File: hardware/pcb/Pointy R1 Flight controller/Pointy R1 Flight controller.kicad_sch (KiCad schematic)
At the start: 9 parts, among them IC1 TEENSY_4.1, Q1 2N7002, Q2 2N7002, Q3 2N7002, U1 L7805CV, U2 GY-521, U3 MPL3115A2

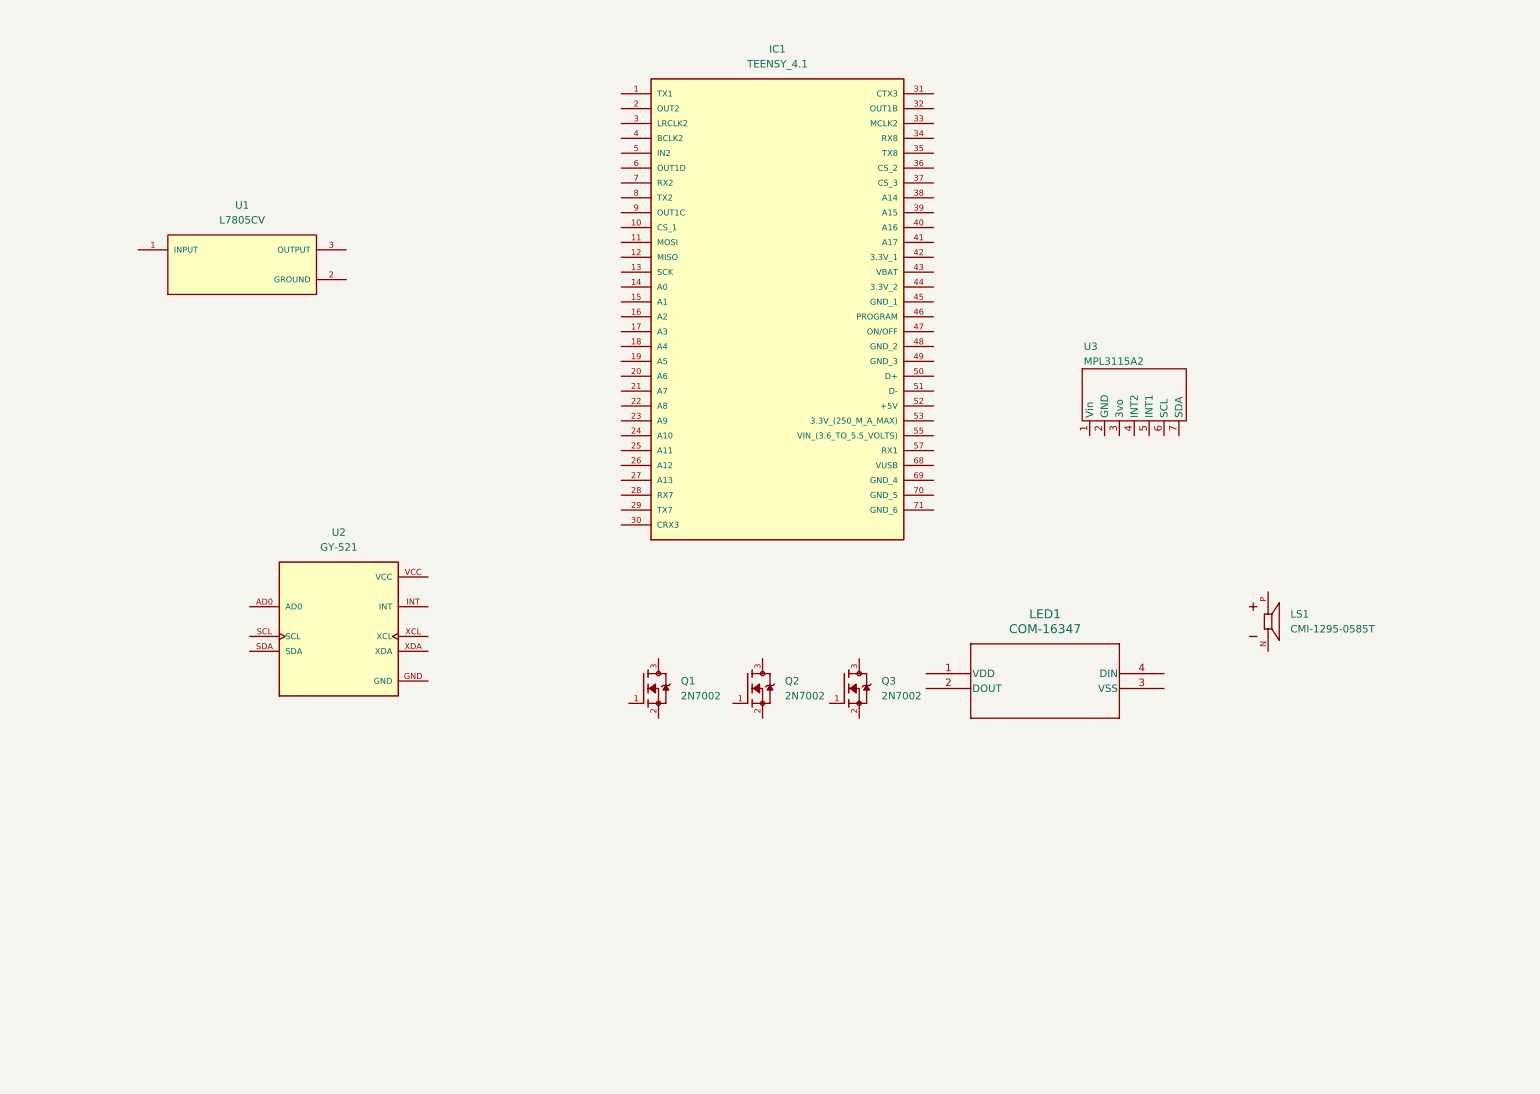
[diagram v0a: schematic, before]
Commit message: added majority of power connections + buses, wired MPL3115A2 altimeter and gy-521 imu
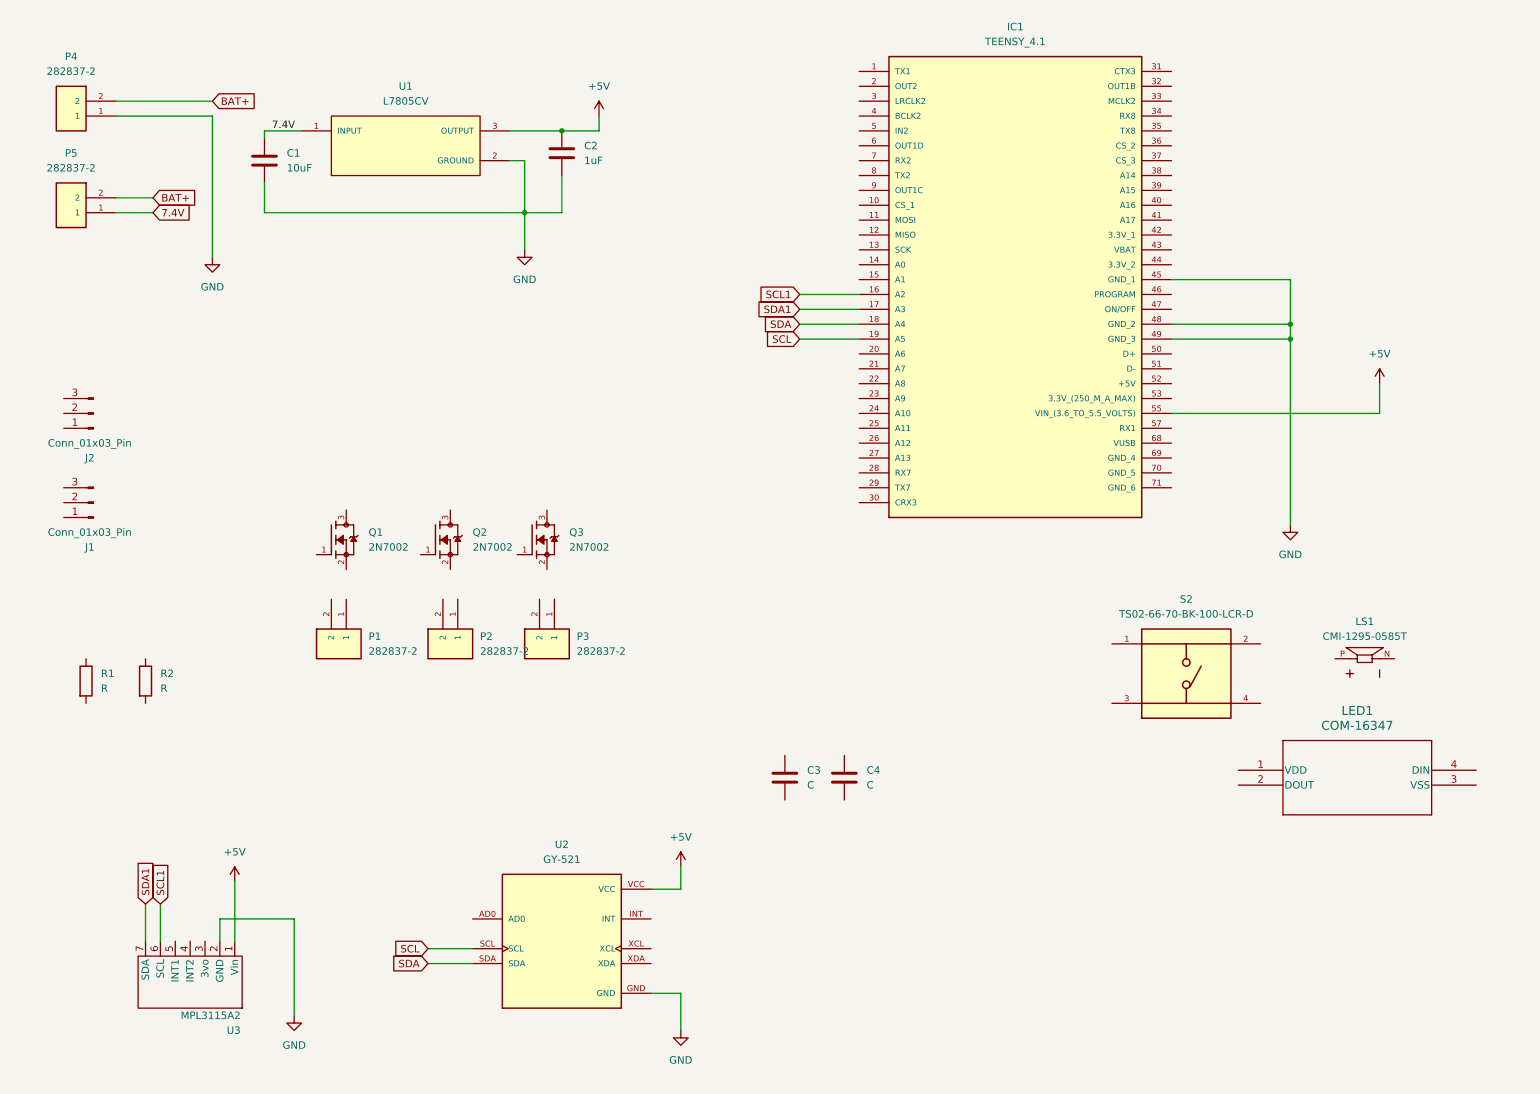
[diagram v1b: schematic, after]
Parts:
- added C1: 10uF, Capacitor_SMD:C_0805_2012Metric, symbol Device:C
- added C2: 1uF, Capacitor_SMD:C_0805_2012Metric, symbol Device:C
- added C3, C4: C, Capacitor_SMD:C_0805_2012Metric, symbol Device:C
- added J1, J2: Conn_01x03_Pin, Connector_PinHeader_2.54mm:PinHeader_1x03_P2.54mm_Vertical, symbol Connector:Conn_01x03_Pin
- added P1, P2, P3, P4, P5: 282837-2, footprints:TE_282837-2, symbol symbols:282837-2
- added R1, R2: R, Resistor_SMD:R_0805_2012Metric, symbol Device:R
- added S2: TS02-66-70-BK-100-LCR-D, footprints:SW_TS02-66-70-BK-100-LCR-D, symbol symbols:TS02-66-70-BK-100-LCR-D
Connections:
- net +5V: now reaches U3.1 (Vin)
- net +5V: now also IC1.55 (VIN_(3.6_TO_5.5_VOLTS)), U1.3 (OUTPUT), U2.VCC, C2.1
- net GND: now reaches U3.2 (GND)
- net GND: now also IC1.45 (GND_1), IC1.48 (GND_2), IC1.49 (GND_3), U1.2 (GROUND), U2.GND, C1.2, C2.2, P4.1
- net SCL1: now reaches U3.6 (SCL)
- net SCL1: now also IC1.16 (A2)
- net SDA1: now reaches U3.7 (SDA)
- net SDA1: now also IC1.17 (A3)
- net 7.4V: now reaches U1.1 (INPUT)
- net 7.4V: now also C1.1, P5.1
- net SCL: now reaches U2.SCL
- net SCL: now also IC1.19 (A5)
- net SDA: now reaches U2.SDA
- net SDA: now also IC1.18 (A4)
- new net BAT+: P4.2, P5.2
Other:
- moved on the sheet: IC1, LED1, LS1, Q1, Q2, Q3, U1, U2, U3

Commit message: added servos, pyro channels, voltage divider, switch, led, buzzer and xt60 connector. Made all connections
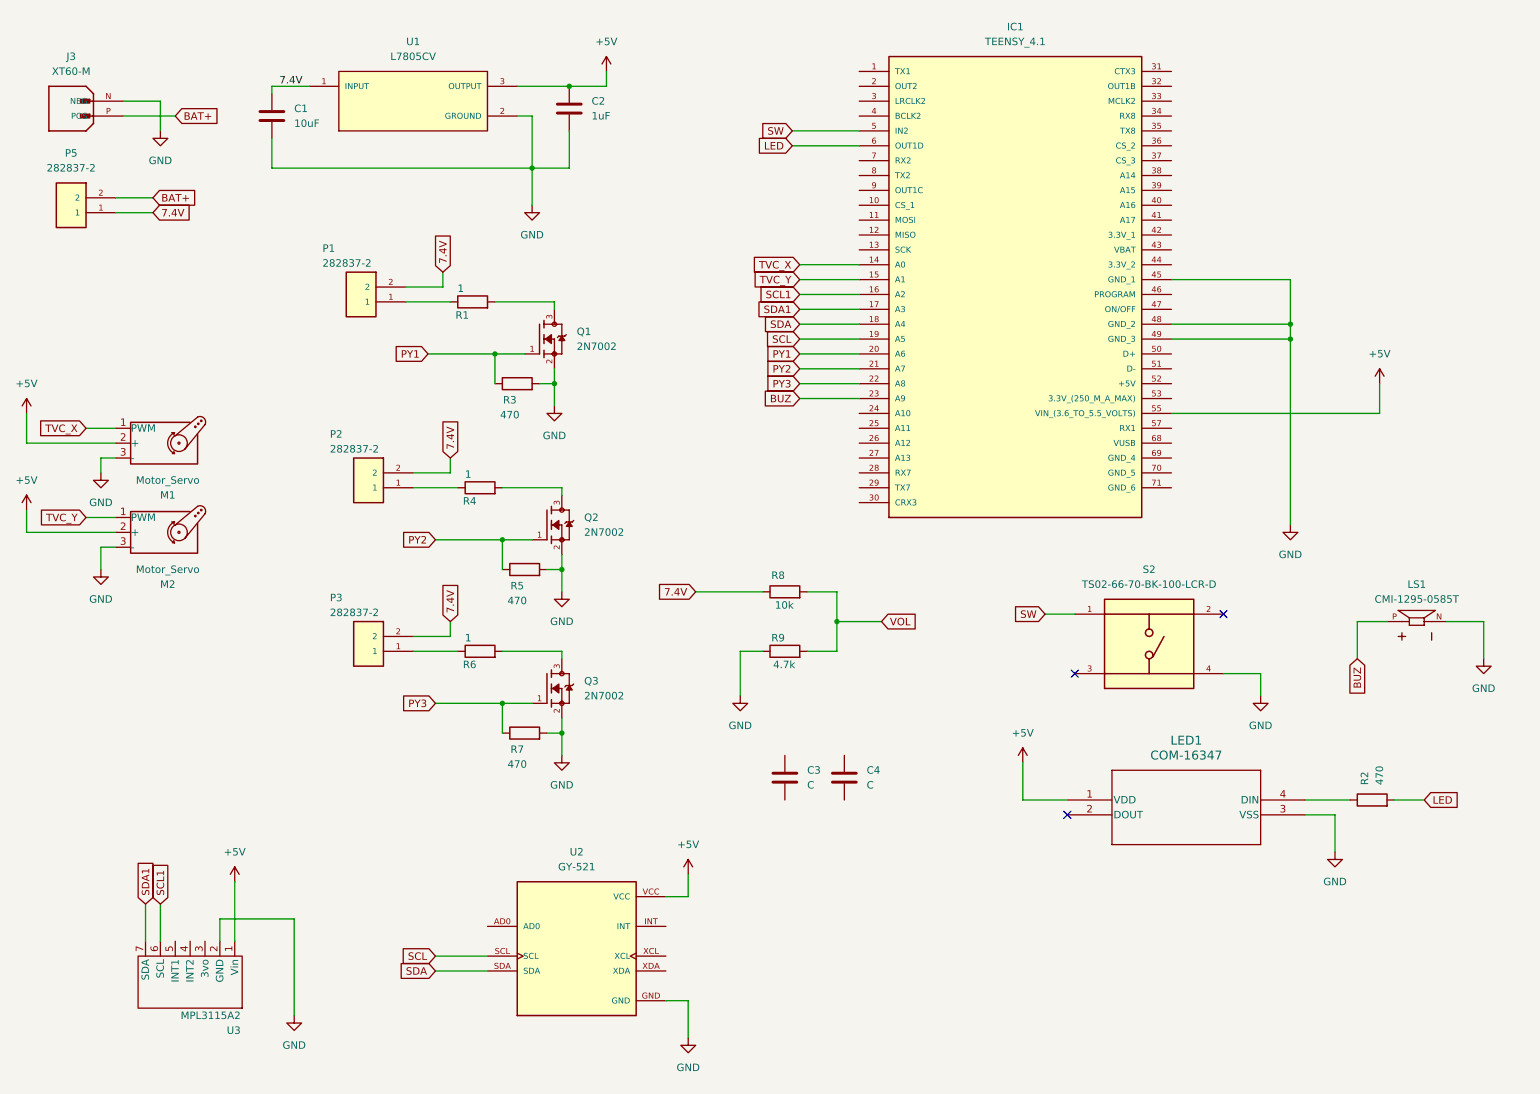
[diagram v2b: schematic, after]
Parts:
- removed J1, J2: Conn_01x03_Pin, Connector_PinHeader_2.54mm:PinHeader_1x03_P2.54mm_Vertical, symbol Connector:Conn_01x03_Pin
- removed P4: 282837-2, footprints:TE_282837-2, symbol symbols:282837-2
- added J3: XT60-M, footprints:AMASS_XT60-M, symbol symbols:XT60-M
- added M1: Motor_Servo, Connector_PinHeader_2.54mm:PinHeader_1x03_P2.54mm_Vertical, symbol Motor:Motor_Servo
- added M2: Motor_Servo, symbol Motor:Motor_Servo
- added R3, R5, R7: 470, Resistor_SMD:R_0805_2012Metric, symbol Device:R
- added R4, R6: 1, Resistor_SMD:R_0805_2012Metric, symbol Device:R
- added R8: 10k, Resistor_SMD:R_0805_2012Metric, symbol Device:R
- added R9: 4.7k, Resistor_SMD:R_0805_2012Metric, symbol Device:R
- R1: value R -> 1
- R2: value R -> 470
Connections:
- net +5V: now also LED1.1 (VDD), M1.2 (+), M2.2 (+)
- net 7.4V: now also P1.2, P2.2, P3.2, R8.1
- net BAT+: now also J3.P (POS)
- net GND: now also LED1.3 (VSS), LS1.N, Q1.2, Q2.2, Q3.2, S2.4, J3.N (NEG), M1.3 (-), M2.3 (-), R3.2, R5.2, R7.2, R9.1
- net at P3.1: now also R6.1
- net at P1.1: now also R1.1
- net PY1: now reaches Q1.1
- net PY1: now also IC1.20 (A6), R3.1
- net at Q1.3: now also R1.2
- net TVC_X: now reaches IC1.14 (A0)
- net TVC_X: now also M1.1 (PWM)
- net TVC_Y: now reaches IC1.15 (A1)
- net TVC_Y: now also M2.1 (PWM)
- net PY2: now reaches IC1.21 (A7)
- net PY2: now also Q2.1, R5.1
- net PY3: now reaches IC1.22 (A8)
- net PY3: now also Q3.1, R7.1
- net BUZ: now reaches IC1.23 (A9)
- net BUZ: now also LS1.P
- net SW: now reaches IC1.5 (IN2)
- net SW: now also S2.1
- net LED: now reaches IC1.6 (OUT1D)
- net LED: now also R2.2
- net at Q2.3: now also R4.2
- net at R2.1: now also LED1.4 (DIN)
- net at Q3.3: now also R6.2
- net at P2.1: now also R4.1
- new net VOL: R8.2, R9.2
- no-connect marks 0 -> 3
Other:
- moved on the sheet: C1, C2, LED1, LS1, P1, Q1, R1, R2, S2, U1, U2

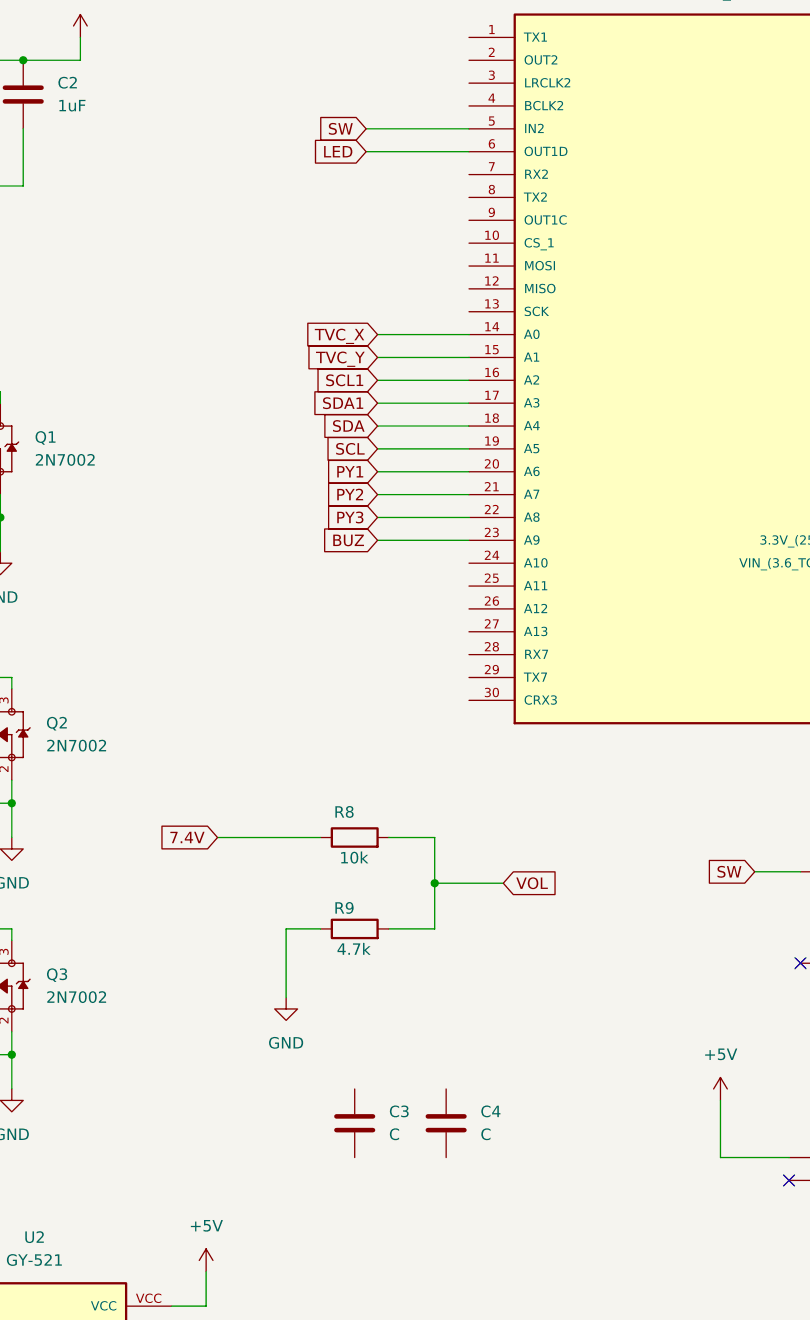
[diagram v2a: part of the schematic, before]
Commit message: Connected voltage divider + removed floating Capacitors
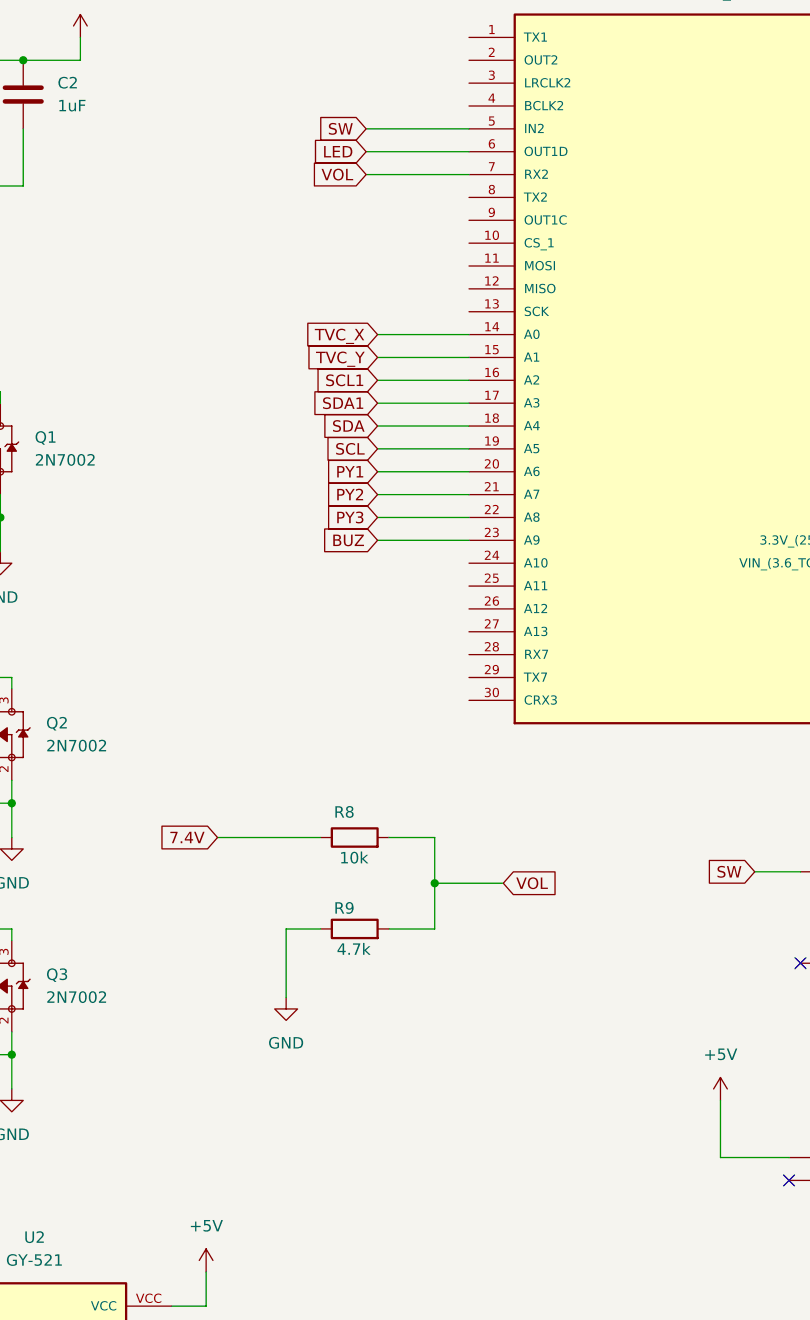
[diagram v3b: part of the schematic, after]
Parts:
- removed C3, C4: C, Capacitor_SMD:C_0805_2012Metric, symbol Device:C
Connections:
- net VOL: now also IC1.7 (RX2)
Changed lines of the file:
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@@
+	(wire
+		(pts
+			(xy 151.13 38.1) (xy 162.56 38.1)
+		)
+		(stroke
+			(width 0)
+			(type default)
+		)
+	)
 	(wire
 		(pts
@@
 		(property "Intersheetrefs" "${INTERSHEET_REFS}"
 			(at 83.6772 173.99 0)
+			(effects
+				(font
+					(size 1.27 1.27)
+				)
+				(justify right)
+				(hide yes)
+			)
+		)
+	)
+	(global_label "VOL"
+		(shape input)
+		(at 151.13 38.1 180)
+		(fields_autoplaced yes)
+		(effects
+			(font
+				(size 1.27 1.27)
+			)
+			(justify right)
+		)
+		(property "Intersheetrefs" "${INTERSHEET_REFS}"
+			(at 144.6976 38.1 0)
 			(effects
 				(font
@@
 	)
 	(symbol
-		(lib_id "Device:C")
-		(at 160.02 143.51 0)
-		(unit 1)
-		(exclude_from_sim no)
-		(in_bom yes)
-		(on_board yes)
-		(dnp no)
-		(fields_autoplaced yes)
-		(property "Reference" "C4"
-			(at 163.83 142.2399 0)
-			(effects
-				(font
-					(size 1.27 1.27)
-				)
-				(justify left)
-			)
-		)
-		(property "Value" "C"
-			(at 163.83 144.7799 0)
-			(effects
-				(font
-					(size 1.27 1.27)
-				)
-				(justify left)
-			)
-		)
-		(property "Footprint" "Capacitor_SMD:C_0805_2012Metric"
-			(at 160.9852 147.32 0)
-			(effects
-				(font
-					(size 1.27 1.27)
-				)
-				(hide yes)
-			)
-		)
-		(property "Datasheet" "~"
-			(at 160.02 143.51 0)
-			(effects
-				(font
-					(size 1.27 1.27)
-				)
-				(hide yes)
-			)
-		)
-		(property "Description" "Unpolarized capacitor"
-			(at 160.02 143.51 0)
-			(effects
-				(font
-					(size 1.27 1.27)
-				)
-				(hide yes)
-			)
-		)
-		(pin "1"
-		)
-		(pin "2"
-		)
-		(instances
-			(project "Pointy R1 Flight controller"
-				(path "/461b38ed-136a-4336-8029-84a41326c46a"
-					(reference "C4")
-					(unit 1)
-				)
-			)
-		)
-	)
-	(symbol
 		(lib_id "power:GND")
 		(at 142.24 129.54 0)
@@
 					(unit 1)
 				)
-			)
-		)
-	)
-	(symbol
-		(lib_id "Device:C")
-		(at 149.86 143.51 0)
-		(unit 1)
-		(exclude_from_sim no)
-		(in_bom yes)
-		(on_board yes)
-		(dnp no)
-		(fields_autoplaced yes)
-		(property "Reference" "C3"
-			(at 153.67 142.2399 0)
-			(effects
-				(font
-					(size 1.27 1.27)
-				)
-				(justify left)
-			)
-		)
-		(property "Value" "C"
-			(at 153.67 144.7799 0)
-			(effects
-				(font
-					(size 1.27 1.27)
-				)
-				(justify left)
-			)
-		)
-		(property "Footprint" "Capacitor_SMD:C_0805_2012Metric"
-			(at 150.8252 147.32 0)
-			(effects
-				(font
-					(size 1.27 1.27)
-				)
-				(hide yes)
-			)
-		)
-		(property "Datasheet" "~"
-			(at 149.86 143.51 0)
-			(effects
-				(font
-					(size 1.27 1.27)
-				)
-				(hide yes)
-			)
-		)
-		(property "Description" "Unpolarized capacitor"
-			(at 149.86 143.51 0)
-			(effects
-				(font
-					(size 1.27 1.27)
-				)
-				(hide yes)
-			)
-		)
-		(pin "1"
-		)
-		(pin "2"
-		)
-		(instances
-			(project "Pointy R1 Flight controller"
-				(path "/461b38ed-136a-4336-8029-84a41326c46a"
-					(reference "C3")
-					(unit 1)
-				)
